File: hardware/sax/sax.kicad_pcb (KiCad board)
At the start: 4 copper layers, 80 x 39 mm, 100 parts, among them J101 Cortex_Debug, J102 JAE_DX07S016JA3, J1101 NE8FAH, J1301 2x05_Horizontal, SW101 SW_Push, SW102 SW_Push, U101 TPS78433QWDRBRQ1, U102 ATSAMD51J, U1101 THVD24x2, U1201 TPSM33625, U1401 BMM150, U1402 BHI160, Y101 32k768

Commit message: Update library
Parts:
- C101, C102, C103, C104, C105, C106, C107, C110, C1101, C111, C1202, C1205, C1401, C1402, C1403, C1404, C1501, C1601, C1701, C1801, C1901, C2001, C2101: footprint Capacitor_SMD:C_0603_1608Metric -> V2_Capacitor_SMD:C_0603
- C108, C109: footprint Capacitor_SMD:C_0805_2012Metric -> V2_Capacitor_SMD:C_0805
- C1201, C1203, C1204: footprint Capacitor_SMD:C_1210_3225Metric -> V2_Capacitor_SMD:C_1210
- D103: footprint LED_SMD:LED_0603_1608Metric -> V2_LED:LED_0603
- D104, D105, D106: value PMEG3010ER -> PMEG6030AEXEX; footprint V2_Diode_SMD:Nexperia_CFP3_SOD-123W -> V2_Diode_SMD:D_SOD-123HP
- FID101, FID102, FID103: value Fiducial -> Fiducial_Paste
- ICON101: footprint V2_Artwork:Logo_Tiny -> V2_Artwork:Logo_Small
- J102: value JAE_DX07S016JA3 -> DX07S016JA3
- R101, R102, R103, R104, R1101, R1201, R1202, R1401, R1402, R1403, R1404, R1405, R1406, R1501, R1502, R1601, R1602, R1701, R1702, R1801, R1802, R1901, R1902, R2001, R2002, R2101, R2102: footprint Resistor_SMD:R_0603_1608Metric -> V2_Resistor_SMD:R_0603
- SW101, SW102: value SW_Push -> SKSG
- TVS101: renamed from TVS102; value SMAJ36CA -> SMBJ36CA; footprint Diode_SMD:D_SMA -> V2_Diode_SMD:D_SMB
- TVS1301, TVS1401, TVS1501, TVS1601, TVS1701, TVS1801, TVS1901, TVS2001, TVS2101: footprint Diode_SMD:D_0603_1608Metric -> V2_Diode_SMD:D_0603
- U1101: value THVD24x2 -> THVD2442
- moved C111 0.75 mm to (77.0, 88.5)
- moved ICON101 0.56 mm to (138.8, 84.2)
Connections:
- net USB-Shield renamed Shield

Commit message: Add sax2
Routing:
- net /Analog-5: track 19.7 -> 18.2 mm
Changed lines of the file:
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@@
 		(layer "F.Fab")
 	)
+	(gr_line
+		(start 137.5 100.25)
+		(end 101.25 100.25)
+		(stroke
+			(width 0.15)
+			(type dot)
+		)
+		(layer "F.Fab")
+	)
 	(dimension
 		(type orthogonal)
@@
 	)
 	(segment
-		(start 92 105.45)
-		(end 92 98.7)
-		(width 0.2)
-		(layer "F.Cu")
-		(net 47)
-	)
-	(segment
-		(start 98.3 109.15)
-		(end 95.7 109.15)
-		(width 0.2)
-		(layer "F.Cu")
-		(net 47)
-	)
-	(segment
 		(start 99.775 110.75)
 		(end 101.175 110.75)
@@
 	)
 	(segment
-		(start 95.7 109.15)
-		(end 92 105.45)
+		(start 99.775 110.75)
+		(end 99.75 110.75)
 		(width 0.2)
 		(layer "F.Cu")
@@
 	)
 	(segment
-		(start 99.775 110.625)
-		(end 98.3 109.15)
+		(start 92 103)
+		(end 92 98.7)
 		(width 0.2)
 		(layer "F.Cu")
@@
 	(segment
 		(start 99.775 110.75)
-		(end 99.775 110.625)
+		(end 99.775 112.2375)
 		(width 0.2)
 		(layer "F.Cu")
@@
 	)
 	(segment
-		(start 99.775 110.75)
-		(end 99.775 112.2375)
+		(start 99.75 110.75)
+		(end 92 103)
 		(width 0.2)
 		(layer "F.Cu")

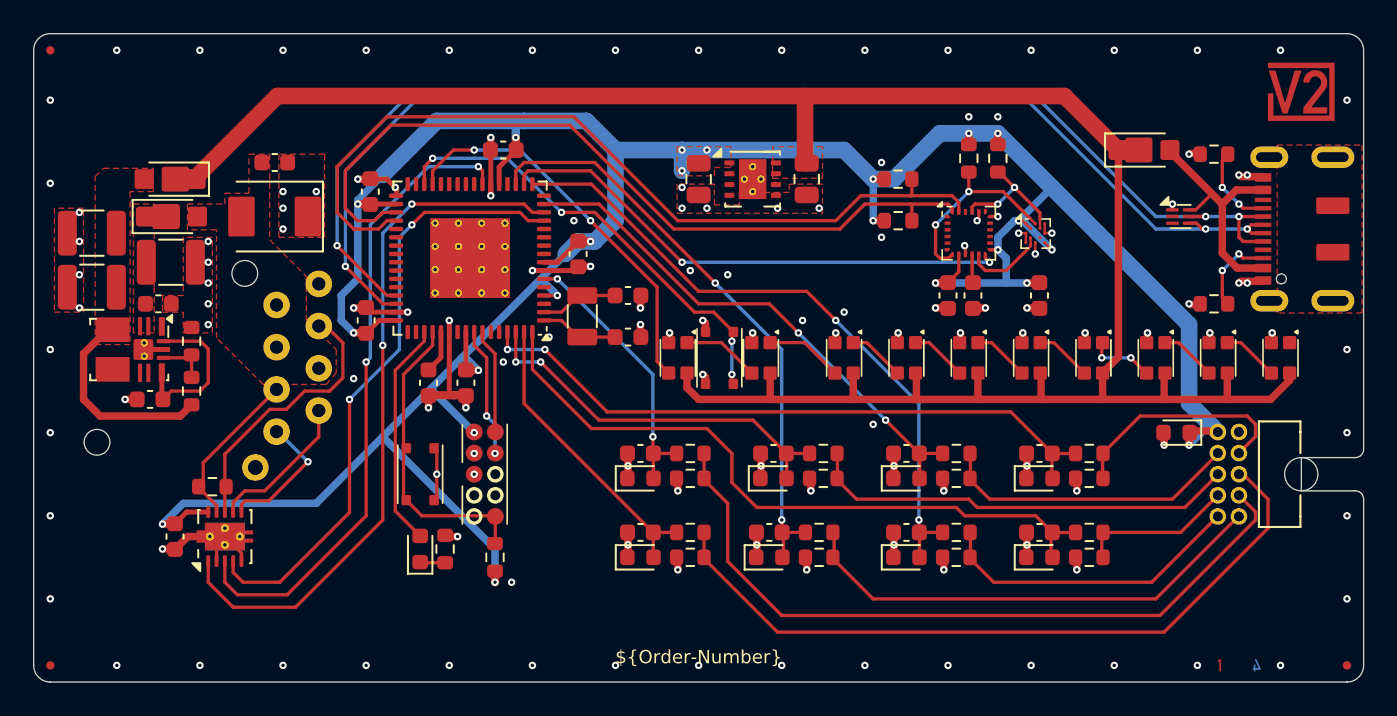
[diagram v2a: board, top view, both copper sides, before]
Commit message: Replace Order_Number
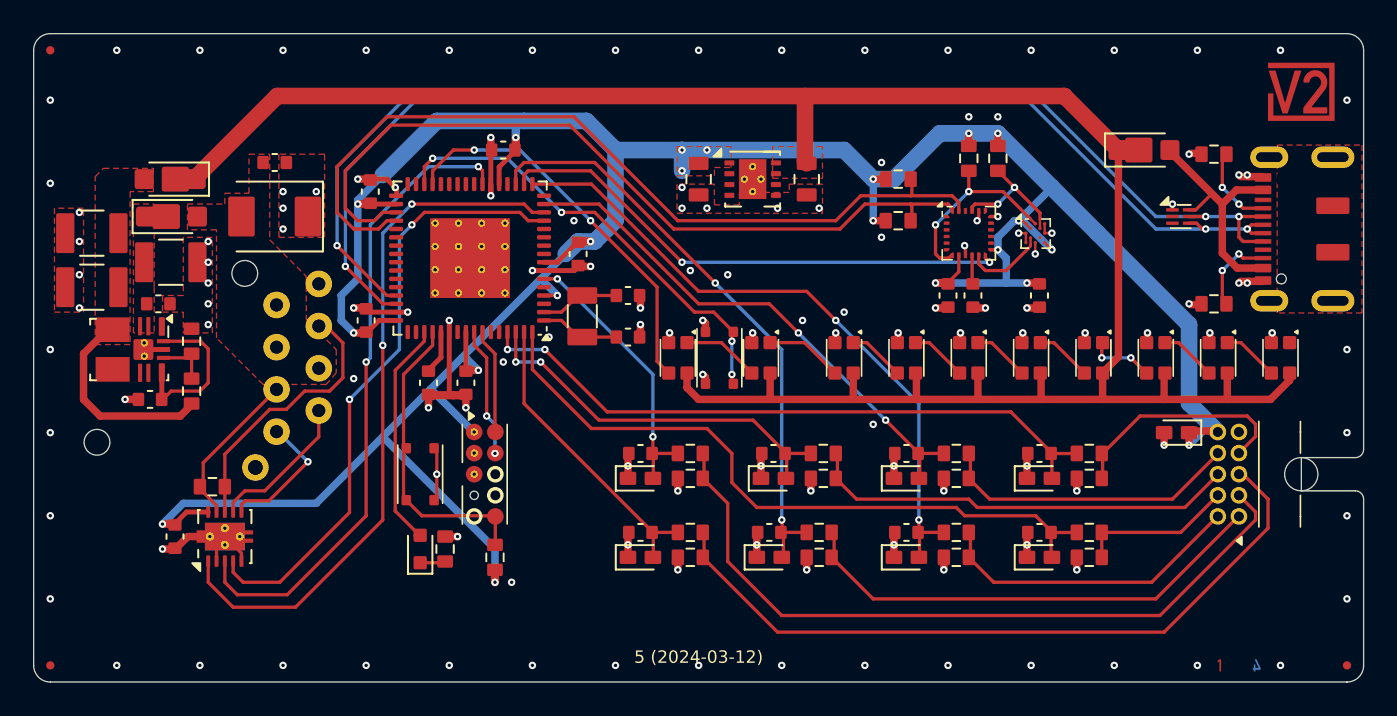
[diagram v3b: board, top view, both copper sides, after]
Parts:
- H101: value MountingHole_2mm -> 2mm
- INFO101: value Order_Number -> ~; footprint V2_Production:Order_Number -> V2_Production:Revision
- J101: value Cortex_Debug -> Cortex; footprint V2_Cortex_Debug:Cortex_Debug_Pad -> V2_Connector_Debug:Cortex
- TVS101: value SMBJ36CA -> SMBJ33CA
- U1201: footprint V2_Converter_DCDC:TPSM33625 -> V2_Converter_DCDC:QFN-11
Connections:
- net +24V renamed +28V
- net /+24V-Link renamed /+28V-Link
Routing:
- net GND: vias 137 -> 135
- net +3V3: vias 22 -> 21

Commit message: Update Library
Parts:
- C1203, C1204: value 22u -> 10u
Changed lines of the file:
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@@
 			)
 		)
-		(property "Value" "22u"
+		(property "Value" "10u"
 			(at 0 2.3 180)
 			(layer "F.Fab")
@@
 			)
 		)
-		(property "Value" "22u"
+		(property "Value" "10u"
 			(at 0 2.3 180)
 			(layer "F.Fab")

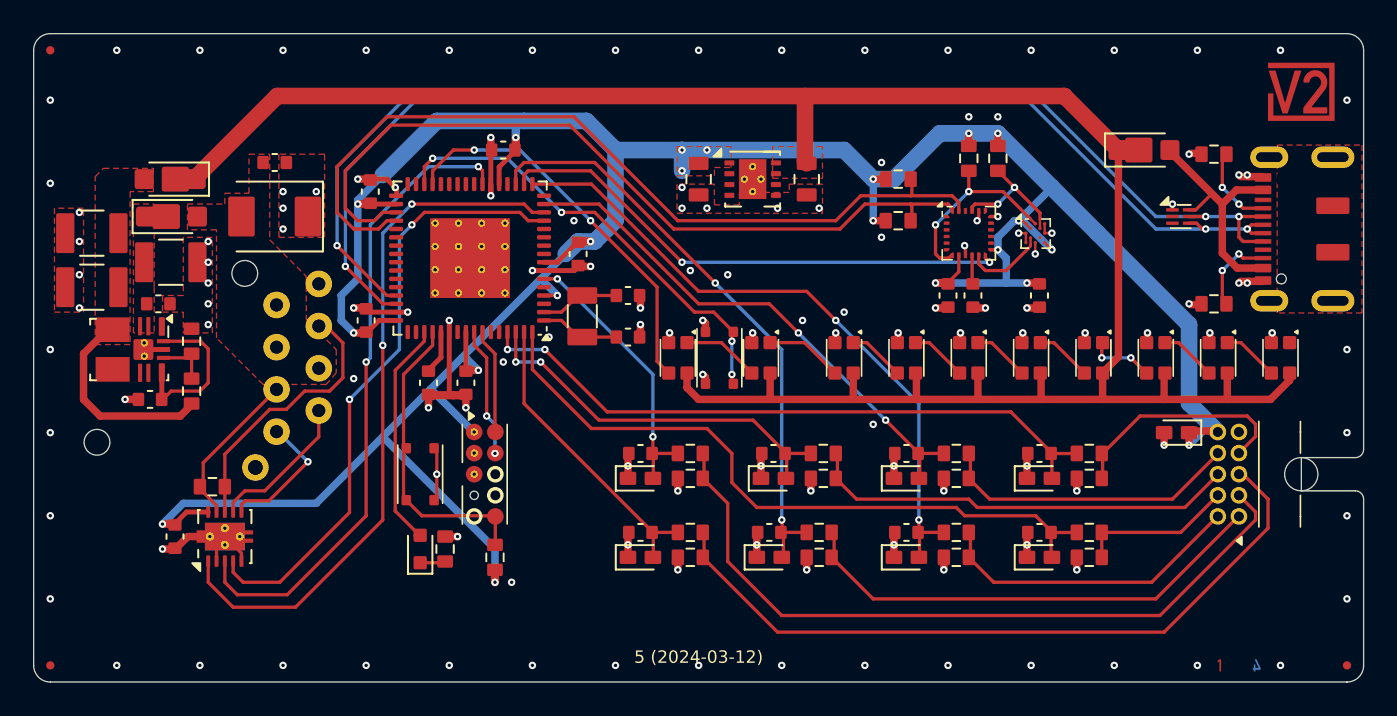
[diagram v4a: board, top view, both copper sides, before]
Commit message: sax2 -> sax
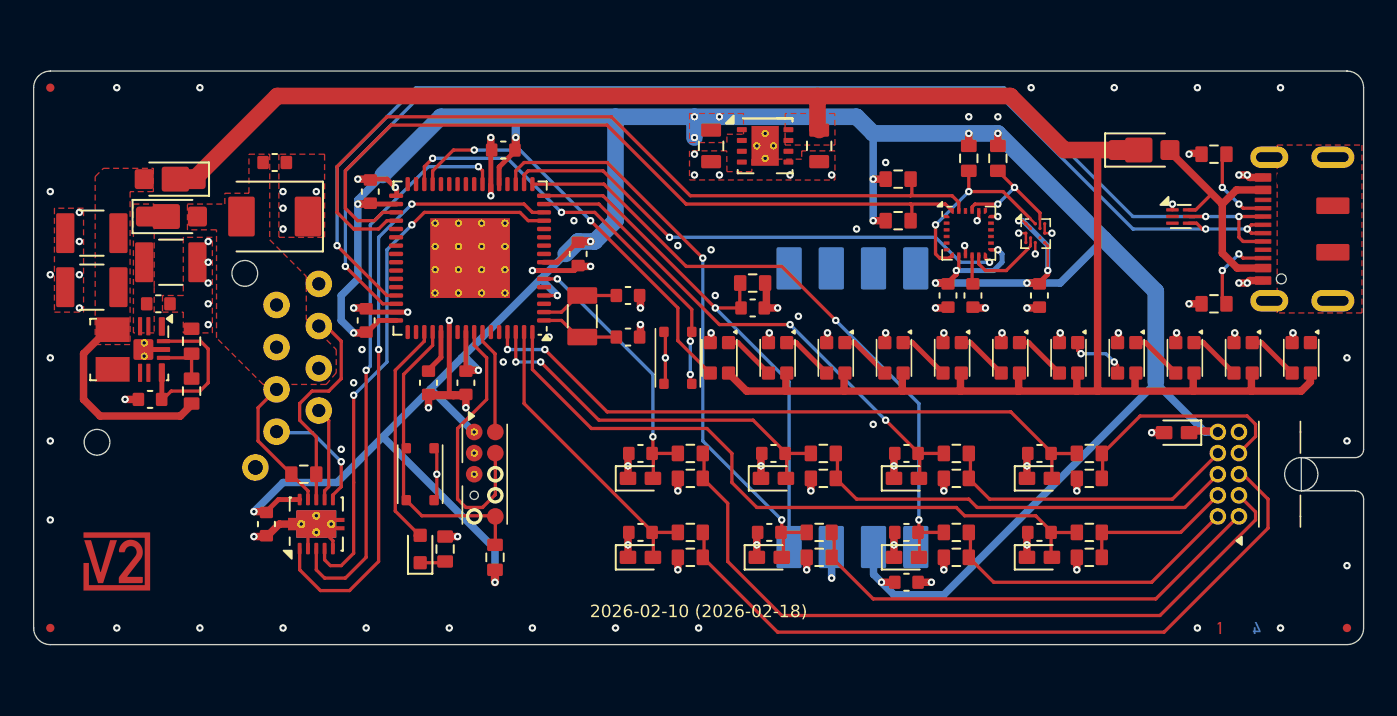
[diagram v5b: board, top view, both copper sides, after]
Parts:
- removed the D101 at (101.2, 100.2)
- added C1402: 0u1, V2_Capacitor_SMD:C_0603, F.Cu at (115.0, 113.8)
- added C1403: 0u022, V2_Capacitor_SMD:C_0603, F.Cu at (105.8, 97.2)
- added D1402: WS2812, V2_LED:WS2812-2020, F.Cu at (110.8, 100.2)
- added D1403: WS2812, V2_LED:WS2812-2020, F.Cu at (107.2, 100.2)
- added IC1401: MP3V5004GP, V2_Sensor_Pressure:MP3V5004GP, B.Cu at (111.8, 103.2)
- added R1404: 100k, V2_Resistor_SMD:R_0603, F.Cu at (105.8, 95.8)
- C1203, C1204: value 10u -> 22u
- U1201: value TPSM33625 -> TPSM365R6FRDNR
- moved ICON101 76.6 mm to (67.5, 112.5)
- moved C1101 5.55 mm to (76.5, 110.2)
- moved R1101 5.55 mm to (78.8, 107.2)
- moved U1101 5.55 mm to (79.5, 110.2)
- moved D1401 3.00 mm to (114.2, 100.2)
- moved D1501 2.75 mm to (117.8, 100.2)
- moved INFO101 2.75 mm to (102.5, 115.5)
- moved D101 2.50 mm to (103.8, 100.2)
- moved D1601 2.50 mm to (121.2, 100.2)
- moved SW101 2.50 mm to (101.2, 100.2)
- moved D1701 2.25 mm to (124.8, 100.2)
- moved FID101 2.25 mm to (63.5, 116.5)
- moved FID102 2.25 mm to (63.5, 84.0)
- moved FID103 2.25 mm to (141.5, 116.5)
- moved INFO102 2.25 mm to (135.0, 116.5)
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- renumbered C1403 to C1404, C1402 to C1405, C1404 to C1406, D102 to D101, D103 to D102, D104 to D103, D105 to D104, D106 to D105, R1402 to R1401, R1403 to R1402, R1401 to R1403, R1404 to R1405, R1405 to R1406, R1406 to R1407
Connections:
- net +28V renamed /+VLINK-Supply
- net /+28V-Link renamed +VLINK
- net /Analog-1 renamed /Hall-1
- net /Analog-2 renamed /Hall-2
- net /Analog-3 renamed /Hall-3
- net /Analog-4 renamed /Hall-4
- net /Analog-5 renamed /Hall-5
- net /Analog-6 renamed /Hall-6
- net /Analog-7 renamed /Hall-7
- net /Analog-8 renamed /Hall-8
- net /Analog/Expression Input 8/LED-Out renamed /Hall Sensors/LED-Out
- net /Analog/LED-2 renamed /Hall Sensors/LED-2
- net /Analog/LED-3 renamed /Hall Sensors/LED-3
- net /Analog/LED-4 renamed /Hall Sensors/LED-4
- net /Analog/LED-5 renamed /Hall Sensors/LED-5
- net /Analog/LED-6 renamed /Hall Sensors/LED-6
- net /Analog/LED-7 renamed /Hall Sensors/LED-7
- net /Analog/LED-8 renamed /Hall Sensors/LED-8
- net /Analog/Sensor-1 renamed /Hall Sensors/Sensor-1
- net /Analog/Sensor-2 renamed /Hall Sensors/Sensor-2
- net /Analog/Sensor-3 renamed /Hall Sensors/Sensor-3
- net /Analog/Sensor-4 renamed /Hall Sensors/Sensor-4
- net /Analog/Sensor-5 renamed /Hall Sensors/Sensor-5
- net /Analog/Sensor-6 renamed /Hall Sensors/Sensor-6
- net /Analog/Sensor-7 renamed /Hall Sensors/Sensor-7
- net /Analog/Sensor-8 renamed /Hall Sensors/Sensor-8
- net /Orientation/Aux-SCK renamed /Orientation Sensor/Aux-SCK
- net /Orientation/Aux-SDA renamed /Orientation Sensor/Aux-SDA
- net /Orientation/MAG-Interrupt renamed /Orientation Sensor/MAG-Interrupt
- net /SCK renamed /SCL
- D101 pad 3: Net-(D101-OUT) -> /LED-Data
- D1401 pad 3: /LED-Sensor -> /LED-Hall
- U102 pad 16: unconnected-(U102-PA07-Pad16) -> /Pressure
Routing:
- net /Pressure: track 0.00 -> 32.3 mm, vias 0 -> 1
- net +3V3: track 184.6 -> 209.9 mm, vias 21 -> 22
- net /SWCLK: track 7.86 -> 16.4 mm, vias 2 -> 0
- net GND: track 73.7 -> 81.3 mm, vias 135 -> 122
- net +5V: track 128.0 -> 121.8 mm
- net /Plug-RX: track 42.5 -> 37.8 mm
- net Net-(D101-OUT): track 4.66 -> 0.00 mm
- net /Plug-TX-Enable: track 38.8 -> 34.2 mm
- net /Plug-TX: track 37.0 -> 32.5 mm
- net /Link Plug/RX-B: track 16.6 -> 13.3 mm
- net /Link Plug/TX-Z: track 8.99 -> 5.71 mm
- net /LED-Pressure: track 0.00 -> 3.16 mm
- net /LED-Hall: track 0.00 -> 3.16 mm
- net /Button: track 27.4 -> 25.7 mm
- net /Link Plug/RX-A: track 9.94 -> 8.38 mm
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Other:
- board size 80 x 39 mm -> 80 x 34.5 mm

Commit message: Refresh
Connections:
- net /VBUS renamed +VBUS
